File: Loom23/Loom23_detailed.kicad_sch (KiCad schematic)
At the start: 7 parts

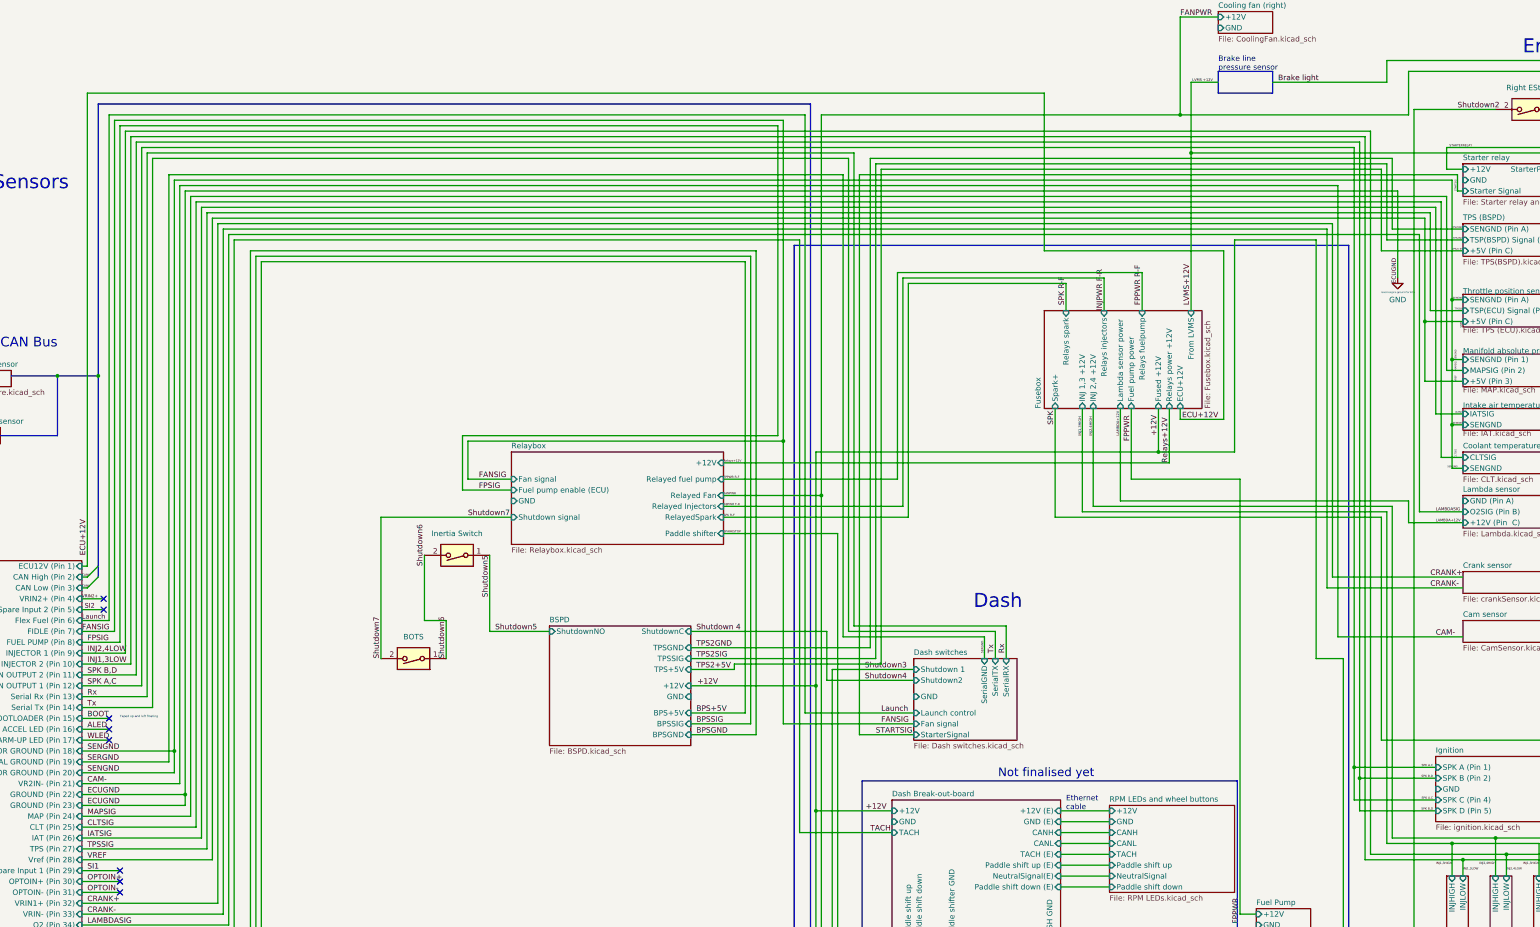
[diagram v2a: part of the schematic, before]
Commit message: Changed labels to match in schematic and spreadsheet
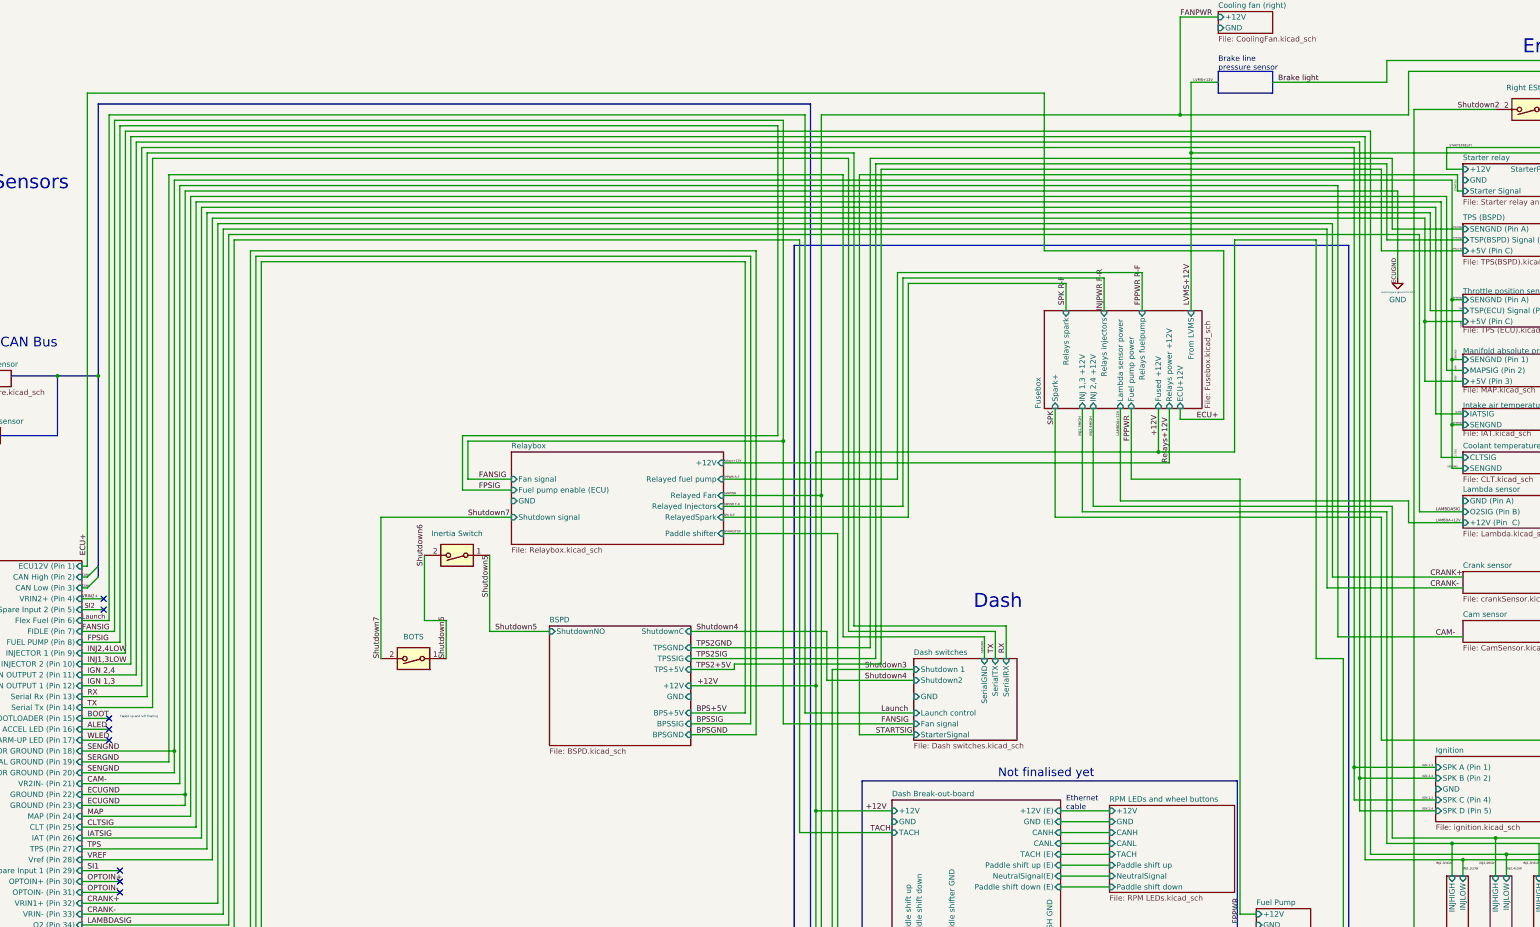
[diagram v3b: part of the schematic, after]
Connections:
- net LVMS +12V renamed LVMS+12V
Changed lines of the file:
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@@
     (effects (font (size 0.5 0.5)) (justify right bottom))
   )
-  (label "FPPWR " (at 332.74 237.49 270)
+  (label "FPPWR" (at 332.74 237.49 270)
     (effects (font (size 1.27 1.27)) (justify right bottom))
   )
@@
     (effects (font (size 0.4 0.4)) (justify left bottom))
   )
-  (label "SPK B,D" (at 377.825 217.17 180)
+  (label "IGN 2,4" (at 377.825 217.17 180)
     (effects (font (size 0.5 0.5)) (justify right bottom))
   )
@@
     (effects (font (size 1.27 1.27)) (justify left bottom))
   )
-  (label "SPK A,C" (at 63.5 187.96 0)
-    (effects (font (size 1.27 1.27)) (justify left bottom))
-  )
-  (label "Tx" (at 275.59 180.34 90)
+  (label "IGN 1,3" (at 63.5 187.96 0)
+    (effects (font (size 1.27 1.27)) (justify left bottom))
+  )
+  (label "TX" (at 275.59 180.34 90)
     (effects (font (size 1.27 1.27)) (justify left bottom))
   )
@@
     (effects (font (size 1.27 1.27)) (justify left bottom))
   )
-  (label "ECU+12V" (at 327.66 125.73 180)
+  (label "ECU+" (at 327.66 125.73 180)
     (effects (font (size 1.27 1.27)) (justify right bottom))
   )
@@
     (effects (font (size 1.27 1.27)) (justify left bottom))
   )
-  (label "SPK B,D" (at 377.825 209.55 180)
-    (effects (font (size 0.5 0.5)) (justify right bottom))
-  )
-  (label "Tx" (at 63.5 193.04 0)
-    (effects (font (size 1.27 1.27)) (justify left bottom))
-  )
-  (label "TPSSIG" (at 63.5 226.06 0)
-    (effects (font (size 1.27 1.27)) (justify left bottom))
-  )
-  (label "SPK B,D" (at 63.5 185.42 0)
+  (label "IGN 2,4" (at 377.825 209.55 180)
+    (effects (font (size 0.5 0.5)) (justify right bottom))
+  )
+  (label "TX" (at 63.5 193.04 0)
+    (effects (font (size 1.27 1.27)) (justify left bottom))
+  )
+  (label "TPS" (at 63.5 226.06 0)
+    (effects (font (size 1.27 1.27)) (justify left bottom))
+  )
+  (label "IGN 2,4" (at 63.5 185.42 0)
     (effects (font (size 1.27 1.27)) (justify left bottom))
   )
@@
     (effects (font (size 0.5 0.5)) (justify left bottom))
   )
-  (label "MAPSIG" (at 63.5 218.44 0)
+  (label "MAP" (at 63.5 218.44 0)
     (effects (font (size 1.27 1.27)) (justify left bottom))
   )
@@
     (effects (font (size 1.27 1.27)) (justify left bottom))
   )
-  (label "LVMS +12V" (at 326.39 46.99 180)
+  (label "LVMS+12V" (at 326.39 46.99 180)
     (effects (font (size 0.6 0.6)) (justify right bottom))
   )
@@
     (effects (font (size 0.5 0.5)) (justify left bottom))
   )
-  (label "FPPWR " (at 307.34 130.81 90)
+  (label "FPPWR" (at 307.34 130.81 90)
     (effects (font (size 1.27 1.27)) (justify left bottom))
   )
@@
     (effects (font (size 1.27 1.27)) (justify left bottom))
   )
-  (label "SPK A,C" (at 377.825 214.63 180)
+  (label "IGN 1,3" (at 377.825 214.63 180)
     (effects (font (size 0.5 0.5)) (justify right bottom))
   )
@@
     (effects (font (size 1.27 1.27)) (justify left bottom))
   )
-  (label "MAPSIG" (at 383.54 114.3 90)
+  (label "MAP" (at 383.54 114.3 90)
     (effects (font (size 0.4 0.4)) (justify left bottom))
   )
@@
     (effects (font (size 1.27 1.27)) (justify left bottom))
   )
-  (label "Shutdown 4" (at 205.74 175.26 0)
+  (label "Shutdown4" (at 205.74 175.26 0)
     (effects (font (size 1.27 1.27)) (justify left bottom))
   )
@@
     (effects (font (size 1.27 1.27)) (justify left bottom))
   )
-  (label "Rx" (at 278.13 180.34 90)
+  (label "RX" (at 278.13 180.34 90)
     (effects (font (size 1.27 1.27)) (justify left bottom))
   )
@@
     (effects (font (size 0.5 0.5)) (justify left bottom))
   )
-  (label "SPK A,C" (at 377.825 207.01 180)
+  (label "IGN 1,3" (at 377.825 207.01 180)
     (effects (font (size 0.5 0.5)) (justify right bottom))
   )
@@
     (effects (font (size 1.27 1.27)) (justify left bottom))
   )
-  (label "TPSSIG" (at 384.81 100.33 180)
+  (label "TPS" (at 384.81 100.33 180)
     (effects (font (size 0.4 0.4)) (justify right bottom))
   )
@@
     (effects (font (size 0.5 0.5)) (justify left bottom))
   )
-  (label "Rx" (at 63.5 190.5 0)
+  (label "RX" (at 63.5 190.5 0)
     (effects (font (size 1.27 1.27)) (justify left bottom))
   )
@@
     (effects (font (size 1.27 1.27)) (justify left bottom))
   )
-  (label "ECU+12V" (at 63.5 157.48 90)
-    (effects (font (size 1.27 1.27)) (justify left bottom))
-  )
+  (label "ECU+" (at 63.5 157.48 90)
+    (effects (font (size 1.27 1.27)) (justify left bottom))
+  )

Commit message: Changes made to fusebox, relayboard and camsensor
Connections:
- no-connect marks 8 -> 7
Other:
- sheet Cam sensor ports: added +5V, CAMSIG, GND; removed none
- sheet Fusebox ports: added Fans, Relays fans; removed Relays power +12V

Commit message: Changed labels to match old wires
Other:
- sheet Dash Break-out-board ports: added CANH (E), CANL (E), NeutralSignal; removed DASH GND, Paddle shifter GND
- sheet Fusebox ports: added FPPWR, Lambda +12V; removed Fuel pump power, Lambda sensor power
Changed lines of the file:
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@@
-    (stroke (width 0) (type default) (color 0 0 0 0))
-  )
-  (wire (pts (xy 265.43 248.92) (xy 265.43 252.73))
     (stroke (width 0) (type default) (color 0 0 0 0))
   )
@@
     (stroke (width 0) (type default) (color 0 0 0 1))
   )
-  (wire (pts (xy 276.86 252.73) (xy 276.86 261.62))
-    (stroke (width 0) (type default) (color 0 0 0 0))
-  )
   (bus (pts (xy 358.14 264.16) (xy 379.73 264.16))
     (stroke (width 0) (type default) (color 0 0 0 0))
@@
     (stroke (width 0) (type default) (color 0 0 0 0))
   )
-  (wire (pts (xy 288.29 267.97) (xy 299.72 267.97))
-    (stroke (width 0) (type default) (color 0 0 0 0))
-  )
   (bus (pts (xy 242.57 271.78) (xy 242.57 274.32))
     (stroke (width 0) (type default) (color 0 0 0 0))
@@
     (stroke (width 0) (type default) (color 0 0 0 1))
   )
-  (wire (pts (xy 265.43 252.73) (xy 276.86 252.73))
-    (stroke (width 0) (type default) (color 0 0 0 0))
-  )
   (wire (pts (xy 271.78 255.27) (xy 271.78 261.62))
     (stroke (width 0) (type default) (color 0 0 0 0))
@@
     (stroke (width 0) (type default) (color 0 0 0 0))
   )
-  (wire (pts (xy 288.29 248.92) (xy 288.29 267.97))
-    (stroke (width 0) (type default) (color 0 0 0 0))
-  )
   (wire (pts (xy 425.45 104.14) (xy 425.45 44.45))
     (stroke (width 0) (type default) (color 0 0 0 0))
@@
     (effects (font (size 1.27 1.27)) (justify left bottom))
   )
+  (label "FANPWR R-F" (at 303.53 100.33 90)
+    (effects (font (size 1.27 1.27)) (justify left bottom))
+  )
   (label "TPS2SIG" (at 205.74 181.61 0)
     (effects (font (size 1.27 1.27)) (justify left bottom))
@@
     (effects (font (size 0.4 0.4)) (justify left bottom))
   )
-  (label "DASHGND" (at 288.29 257.81 90)
-    (effects (font (size 1.27 1.27)) (justify left bottom))
-  )
   (label "FANSIG" (at 154.94 139.7 0)
     (effects (font (size 1.27 1.27)) (justify left bottom))
@@
   (label "INJ2,4HIGH" (at 298.45 129.54 90)
     (effects (font (size 0.6 0.6)) (justify left bottom))
-  )
-  (label "DASHGND" (at 290.83 267.97 0)
-    (effects (font (size 1.27 1.27)) (justify left bottom))
   )
   (label "RX" (at 278.13 180.34 90)
@@
       (effects (font (size 1.27 1.27)) (justify right))
     )
-    (pin "Lambda sensor power" input (at 304.8 123.19 270)
-      (effects (font (size 1.27 1.27)) (justify left))
-    )
     (pin "Relays spark" input (at 292.1 100.33 90)
       (effects (font (size 1.27 1.27)) (justify right))
     )
-    (pin "Fuel pump power" input (at 307.34 123.19 270)
-      (effects (font (size 1.27 1.27)) (justify left))
-    )
     (pin "Relays injectors" input (at 300.99 100.33 90)
       (effects (font (size 1.27 1.27)) (justify right))
@@
     )
     (pin "Fans" input (at 292.1 123.19 270)
+      (effects (font (size 1.27 1.27)) (justify left))
+    )
+    (pin "Lambda +12V" input (at 304.8 123.19 270)
+      (effects (font (size 1.27 1.27)) (justify left))
+    )
+    (pin "FPPWR" input (at 307.34 123.19 270)
       (effects (font (size 1.27 1.27)) (justify left))
     )
@@
       (effects (font (size 1.27 1.27)) (justify left))
     )
-    (pin "DASH GND" input (at 288.29 248.92 270)
-      (effects (font (size 1.27 1.27)) (justify left))
-    )
     (pin "+12V (E)" input (at 290.83 217.17 0)
       (effects (font (size 1.27 1.27)) (justify right))
@@
       (effects (font (size 1.27 1.27)) (justify right))
     )
-    (pin "Paddle shift down" input (at 257.81 248.92 270)
-      (effects (font (size 1.27 1.27)) (justify left))
-    )
-    (pin "Paddle shifter GND" input (at 265.43 248.92 270)
+    (pin "TACH (E)" input (at 290.83 227.33 0)
+      (effects (font (size 1.27 1.27)) (justify right))
+    )
+    (pin "Paddle shift down (E)" input (at 290.83 234.95 0)
+      (effects (font (size 1.27 1.27)) (justify right))
+    )
+    (pin "Paddle shift up (E)" input (at 290.83 229.87 0)
+      (effects (font (size 1.27 1.27)) (justify right))
+    )
+    (pin "NeutralSignal(E)" input (at 290.83 232.41 0)
+      (effects (font (size 1.27 1.27)) (justify right))
+    )
+    (pin "NeutralSignal" input (at 260.35 248.92 270)
+      (effects (font (size 1.27 1.27)) (justify left))
+    )
+    (pin "Paddle shift down" input (at 257.556 248.92 270)
+      (effects (font (size 1.27 1.27)) (justify left))
+    )
+    (pin "CANL" input (at 267.208 248.92 270)
+      (effects (font (size 1.27 1.27)) (justify left))
+    )
+    (pin "CANH" input (at 264.16 248.92 270)
       (effects (font (size 1.27 1.27)) (justify left))
     )
@@
       (effects (font (size 1.27 1.27)) (justify left))
     )
-    (pin "TACH (E)" input (at 290.83 227.33 0)
-      (effects (font (size 1.27 1.27)) (justify right))
-    )
-    (pin "Paddle shift down (E)" input (at 290.83 234.95 0)
-      (effects (font (size 1.27 1.27)) (justify right))
-    )
-    (pin "Paddle shift up (E)" input (at 290.83 229.87 0)
-      (effects (font (size 1.27 1.27)) (justify right))
-    )
-    (pin "NeutralSignal(E)" input (at 290.83 232.41 0)
-      (effects (font (size 1.27 1.27)) (justify right))
-    )
-    (pin "CANH" input (at 290.83 222.25 0)
-      (effects (font (size 1.27 1.27)) (justify right))
-    )
-    (pin "CANL" input (at 290.83 224.79 0)
+    (pin "CANH (E)" input (at 290.83 222.25 0)
+      (effects (font (size 1.27 1.27)) (justify right))
+    )
+    (pin "CANL (E)" input (at 290.83 224.79 0)
       (effects (font (size 1.27 1.27)) (justify right))
     )
@@
       (effects (font (size 1.27 1.27)) (justify left top))
     )
-    (pin "CANH" input (at 281.94 273.05 0)
-      (effects (font (size 1.27 1.27)) (justify right))
-    )
-    (pin "CANL" input (at 281.94 275.59 0)
+    (pin "CANH" input (at 277.114 261.62 90)
+      (effects (font (size 1.27 1.27)) (justify right))
+    )
+    (pin "CANL" input (at 279.654 261.62 90)
       (effects (font (size 1.27 1.27)) (justify right))
     )
@@
       (effects (font (size 1.27 1.27)) (justify left))
     )
-    (pin "GND" input (at 276.86 261.62 90)
-      (effects (font (size 1.27 1.27)) (justify right))
+    (pin "GND" input (at 251.46 267.462 180)
+      (effects (font (size 1.27 1.27)) (justify left))
     )
   )
@@
       (reference "J6") (unit 1) (value "282087-1") (footprint "Additional Footprints:3 pin flying lead")
     )
+    (path "/1d27a9e1-a99a-46d7-b2ea-46112bae4d76/1dbb7395-e64d-428b-a5e5-51d2baccb335"
+      (reference "J?") (unit 1) (value "RJ45") (footprint "Footprints:RJ45_TE_5557789-1")
+    )
+    (path "/1d27a9e1-a99a-46d7-b2ea-46112bae4d76/6ea48b74-ab14-4b09-8e16-c9fda2cfa574"
+      (reference "J?") (unit 1) (value "Conn_01x06_Female") (footprint "Footprints:JST_XA_B06B-XASK-1_1x06_P2.50mm_Vertical")
+    )
     (path "/7b0f0b05-0256-463a-ae57-e387aefb1021/8d81c52c-58bc-4fd5-b235-7cb50677c6d0"
       (reference "J?") (unit 1) (value "AudioJack3") (footprint "")
     )
+    (path "/1d27a9e1-a99a-46d7-b2ea-46112bae4d76/a89de842-e45f-4f66-b932-200994a77154"
+      (reference "J?") (unit 1) (value "Screw_Terminal_01x02") (footprint "TerminalBlock:TerminalBlock_bornier-2_P5.08mm")
+    )
+    (path "/1d27a9e1-a99a-46d7-b2ea-46112bae4d76/e90384fb-8fea-4450-92da-9f4f9e2f5775"
+      (reference "J?") (unit 1) (value "Conn_01x06_Female") (footprint "Footprints:JST_XA_B06B-XASK-1_1x06_P2.50mm_Vertical")
+    )
     (path "/10890e7c-b700-45d3-80f8-41487eb0e501/2c679e06-a412-4f71-b42e-bbaeeb1b794d"
